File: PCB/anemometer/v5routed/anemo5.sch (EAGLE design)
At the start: 77 parts, among them IC1 AD8223, IC2 AD8223, IC3 AD8223, IC4 AD8223, IC5 TL072D, IC6 TL072D, IC7 TL072D, J1 RJ12STRAIGHT-I2C, J2 RJ12STRAIGHT-I2C

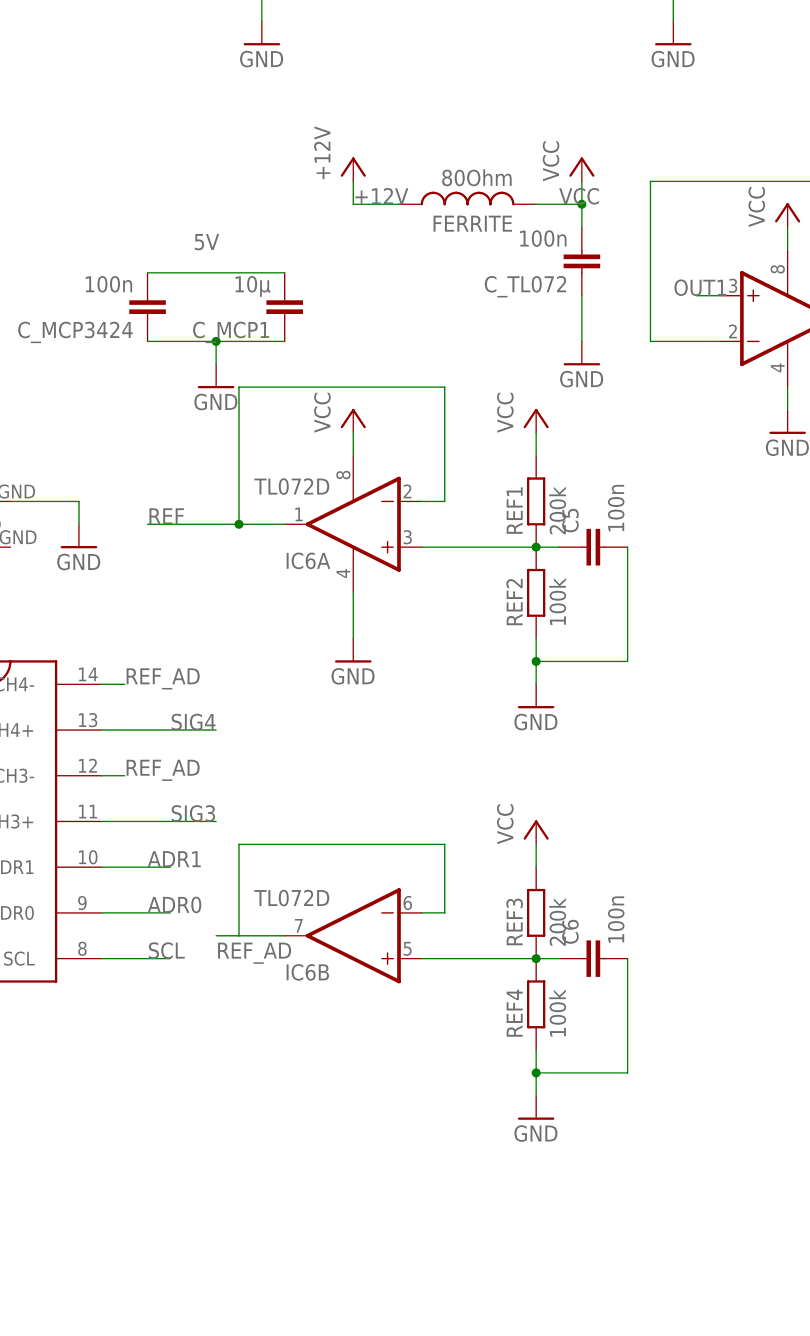
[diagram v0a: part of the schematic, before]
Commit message: created gerber for anemo5
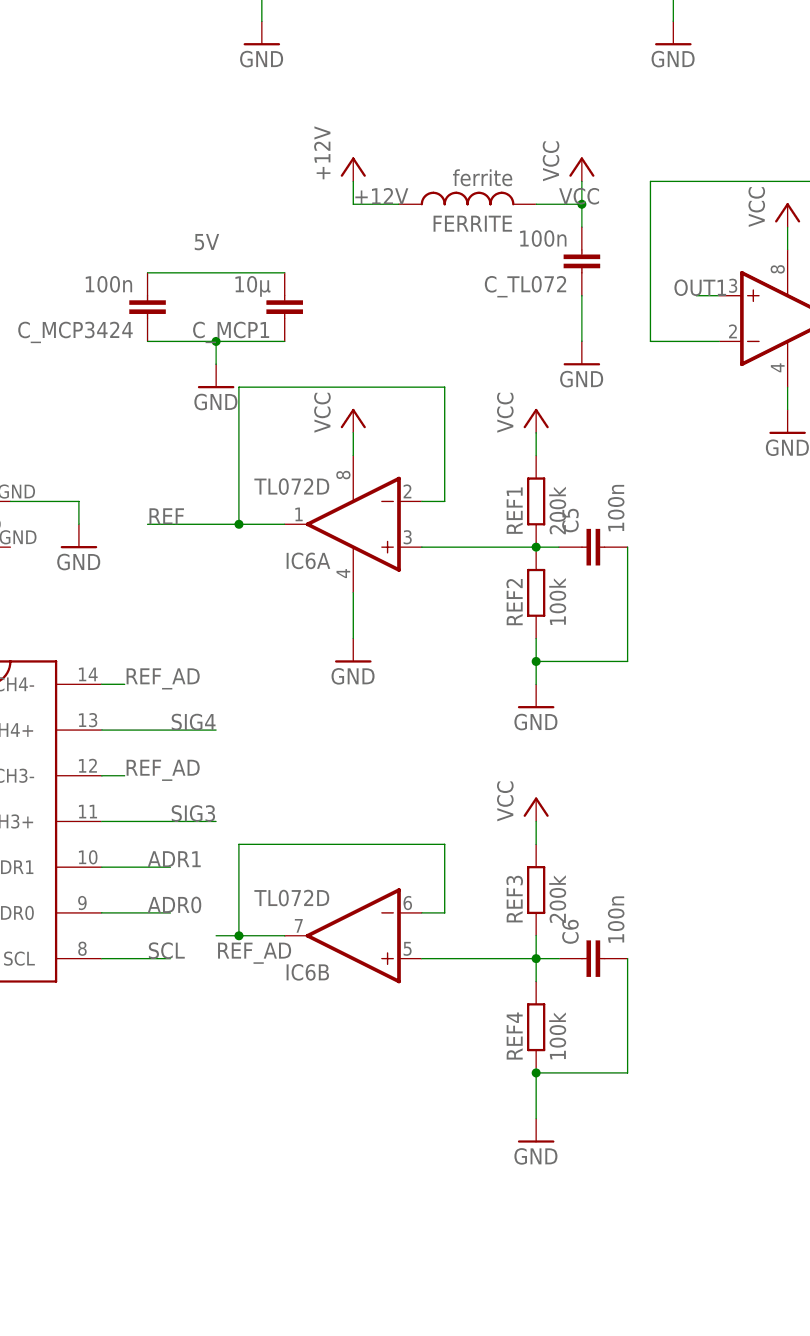
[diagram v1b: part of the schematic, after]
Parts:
- FERRITE: value 80Ohm -> ferrite
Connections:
- net N$24: now also IC6B.+IN
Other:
- moved on the sheet: REF3, REF4
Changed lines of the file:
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@@
 <grid distance="0.1" unitdist="inch" unit="inch" style="lines" multiple="1" display="no" altdistance="0.01" altunitdist="inch" altunit="inch"/>
 <layers>
-<layer number="1" name="Top" color="4" fill="1" visible="yes" active="no"/>
-<layer number="16" name="Bottom" color="1" fill="1" visible="yes" active="no"/>
-<layer number="17" name="Pads" color="2" fill="1" visible="yes" active="no"/>
-<layer number="18" name="Vias" color="2" fill="1" visible="yes" active="no"/>
-<layer number="19" name="Unrouted" color="6" fill="1" visible="yes" active="no"/>
-<layer number="20" name="Dimension" color="15" fill="1" visible="yes" active="no"/>
-<layer number="21" name="tPlace" color="7" fill="1" visible="yes" active="no"/>
-<layer number="22" name="bPlace" color="7" fill="1" visible="yes" active="no"/>
-<layer number="23" name="tOrigins" color="15" fill="1" visible="yes" active="no"/>
-<layer number="24" name="bOrigins" color="15" fill="1" visible="yes" active="no"/>
-<layer number="25" name="tNames" color="7" fill="1" visible="yes" active="no"/>
-<layer number="26" name="bNames" color="7" fill="1" visible="yes" active="no"/>
-<layer number="27" name="tValues" color="7" fill="1" visible="yes" active="no"/>
-<layer number="28" name="bValues" color="7" fill="1" visible="yes" active="no"/>
+<layer number="1" name="Top" color="4" fill="1" visible="no" active="no"/>
+<layer number="16" name="Bottom" color="1" fill="1" visible="no" active="no"/>
+<layer number="17" name="Pads" color="2" fill="1" visible="no" active="no"/>
+<layer number="18" name="Vias" color="2" fill="1" visible="no" active="no"/>
+<layer number="19" name="Unrouted" color="6" fill="1" visible="no" active="no"/>
+<layer number="20" name="Dimension" color="15" fill="1" visible="no" active="no"/>
+<layer number="21" name="tPlace" color="7" fill="1" visible="no" active="no"/>
+<layer number="22" name="bPlace" color="7" fill="1" visible="no" active="no"/>
+<layer number="23" name="tOrigins" color="15" fill="1" visible="no" active="no"/>
+<layer number="24" name="bOrigins" color="15" fill="1" visible="no" active="no"/>
+<layer number="25" name="tNames" color="7" fill="1" visible="no" active="no"/>
+<layer number="26" name="bNames" color="7" fill="1" visible="no" active="no"/>
+<layer number="27" name="tValues" color="7" fill="1" visible="no" active="no"/>
+<layer number="28" name="bValues" color="7" fill="1" visible="no" active="no"/>
 <layer number="29" name="tStop" color="7" fill="3" visible="no" active="no"/>
 <layer number="30" name="bStop" color="7" fill="6" visible="no" active="no"/>
@@
 <layer number="35" name="tGlue" color="7" fill="4" visible="no" active="no"/>
 <layer number="36" name="bGlue" color="7" fill="5" visible="no" active="no"/>
-<layer number="37" name="tTest" color="7" fill="1" visible="yes" active="no"/>
-<layer number="38" name="bTest" color="7" fill="1" visible="yes" active="no"/>
+<layer number="37" name="tTest" color="7" fill="1" visible="no" active="no"/>
+<layer number="38" name="bTest" color="7" fill="1" visible="no" active="no"/>
 <layer number="39" name="tKeepout" color="4" fill="11" visible="no" active="no"/>
 <layer number="40" name="bKeepout" color="1" fill="11" visible="no" active="no"/>
@@
 <layer number="44" name="Drills" color="7" fill="1" visible="no" active="no"/>
 <layer number="45" name="Holes" color="7" fill="1" visible="no" active="no"/>
-<layer number="46" name="Milling" color="3" fill="1" visible="yes" active="no"/>
-<layer number="47" name="Measures" color="7" fill="1" visible="yes" active="no"/>
-<layer number="48" name="Document" color="7" fill="1" visible="yes" active="no"/>
-<layer number="49" name="Reference" color="7" fill="1" visible="yes" active="no"/>
-<layer number="50" name="dxf" color="7" fill="1" visible="yes" active="no"/>
-<layer number="51" name="tDocu" color="7" fill="1" visible="yes" active="no"/>
-<layer number="52" name="bDocu" color="7" fill="1" visible="yes" active="no"/>
-<layer number="53" name="tGND_GNDA" color="7" fill="9" visible="yes" active="no"/>
-<layer number="54" name="bGND_GNDA" color="1" fill="9" visible="yes" active="no"/>
-<layer number="56" name="wert" color="7" fill="1" visible="yes" active="no"/>
+<layer number="46" name="Milling" color="3" fill="1" visible="no" active="no"/>
+<layer number="47" name="Measures" color="7" fill="1" visible="no" active="no"/>
+<layer number="48" name="Document" color="7" fill="1" visible="no" active="no"/>
+<layer number="49" name="Reference" color="7" fill="1" visible="no" active="no"/>
+<layer number="50" name="dxf" color="7" fill="1" visible="no" active="no"/>
+<layer number="51" name="tDocu" color="7" fill="1" visible="no" active="no"/>
+<layer number="52" name="bDocu" color="7" fill="1" visible="no" active="no"/>
+<layer number="53" name="tGND_GNDA" color="7" fill="9" visible="no" active="no"/>
+<layer number="54" name="bGND_GNDA" color="1" fill="9" visible="no" active="no"/>
+<layer number="56" name="wert" color="7" fill="1" visible="no" active="no"/>
 <layer number="91" name="Nets" color="2" fill="1" visible="yes" active="yes"/>
 <layer number="92" name="Busses" color="1" fill="1" visible="yes" active="yes"/>
@@
 <part name="LED0" library="SparkFun" deviceset="LED" device="1206"/>
 <part name="GND26" library="supply1" deviceset="GND" device=""/>
-<part name="FERRITE" library="rcl" deviceset="L-US" device="L3216C" value="80Ohm"/>
+<part name="FERRITE" library="rcl" deviceset="L-US" device="L3216C" value="ferrite"/>
 <part name="P+11" library="supply1" deviceset="VCC" device="" value="+12V"/>
 <part name="GND19" library="supply1" deviceset="GND" device=""/>
@@
 <instance part="RC3" gate="G$1" x="182.88" y="10.16" rot="R90"/>
 <instance part="RC4" gate="G$1" x="223.52" y="10.16" rot="R90"/>
-<instance part="REF3" gate="G$1" x="60.96" y="-73.66" rot="R90"/>
-<instance part="REF4" gate="G$1" x="60.96" y="-83.82" rot="R90"/>
-<instance part="P+14" gate="VCC" x="60.96" y="-63.5"/>
-<instance part="GND22" gate="1" x="60.96" y="-96.52"/>
+<instance part="REF3" gate="G$1" x="60.96" y="-71.12" rot="R90"/>
+<instance part="REF4" gate="G$1" x="60.96" y="-86.36" rot="R90"/>
+<instance part="P+14" gate="VCC" x="60.96" y="-60.96"/>
+<instance part="GND22" gate="1" x="60.96" y="-99.06"/>
 <instance part="C6" gate="G$1" x="66.04" y="-78.74" rot="R90"/>
 </instances>
@@
 <pinref part="REF3" gate="G$1" pin="2"/>
 <pinref part="P+14" gate="VCC" pin="VCC"/>
-<wire x1="60.96" y1="-68.58" x2="60.96" y2="-66.04" width="0.1524" layer="91"/>
+<wire x1="60.96" y1="-66.04" x2="60.96" y2="-63.5" width="0.1524" layer="91"/>
 </segment>
 </net>
@@
 <pinref part="GND22" gate="1" pin="GND"/>
 <pinref part="REF4" gate="G$1" pin="1"/>
-<wire x1="60.96" y1="-93.98" x2="60.96" y2="-91.44" width="0.1524" layer="91"/>
+<wire x1="60.96" y1="-96.52" x2="60.96" y2="-91.44" width="0.1524" layer="91"/>
 <pinref part="C6" gate="G$1" pin="2"/>
-<wire x1="60.96" y1="-91.44" x2="60.96" y2="-88.9" width="0.1524" layer="91"/>
 <wire x1="60.96" y1="-91.44" x2="71.12" y2="-91.44" width="0.1524" layer="91"/>
 <wire x1="71.12" y1="-91.44" x2="71.12" y2="-78.74" width="0.1524" layer="91"/>
@@
 </segment>
 </net>
-<net name="N$24" class="0">
-<segment>
-<wire x1="48.26" y1="-78.74" x2="60.96" y2="-78.74" width="0.1524" layer="91"/>
-<pinref part="REF4" gate="G$1" pin="2"/>
-<pinref part="REF3" gate="G$1" pin="1"/>
-<junction x="60.96" y="-78.74"/>
-<pinref part="C6" gate="G$1" pin="1"/>
-<wire x1="63.5" y1="-78.74" x2="60.96" y2="-78.74" width="0.1524" layer="91"/>
-</segment>
-</net>
 <net name="REF_AD" class="0">
 <segment>
@@
 <wire x1="27.94" y1="-76.2" x2="25.4" y2="-76.2" width="0.1524" layer="91"/>
 <label x="25.4" y="-78.74" size="1.778" layer="95"/>
+<junction x="27.94" y="-76.2"/>
 </segment>
 <segment>
@@
 </segment>
 </net>
+<net name="N$24" class="0">
+<segment>
+<pinref part="C6" gate="G$1" pin="1"/>
+<pinref part="IC6" gate="B" pin="+IN"/>
+<wire x1="63.5" y1="-78.74" x2="60.96" y2="-78.74" width="0.1524" layer="91"/>
+<pinref part="REF3" gate="G$1" pin="1"/>
+<pinref part="REF4" gate="G$1" pin="2"/>
+<wire x1="60.96" y1="-78.74" x2="48.26" y2="-78.74" width="0.1524" layer="91"/>
+<wire x1="60.96" y1="-76.2" x2="60.96" y2="-78.74" width="0.1524" layer="91"/>
+<junction x="60.96" y="-78.74"/>
+<wire x1="60.96" y1="-78.74" x2="60.96" y2="-81.28" width="0.1524" layer="91"/>
+</segment>
+</net>
